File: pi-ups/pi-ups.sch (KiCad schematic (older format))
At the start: 31 parts, among them J1 , Q1 IRLML2244, Q2 IRLML2244, Q3 IRLML2244, Q4 IRLML2244, U1 BMS_1S, U2 DC-DC, U3 BMS_1S, U4 FTDI232, U5 Arduino_Pro_Mini

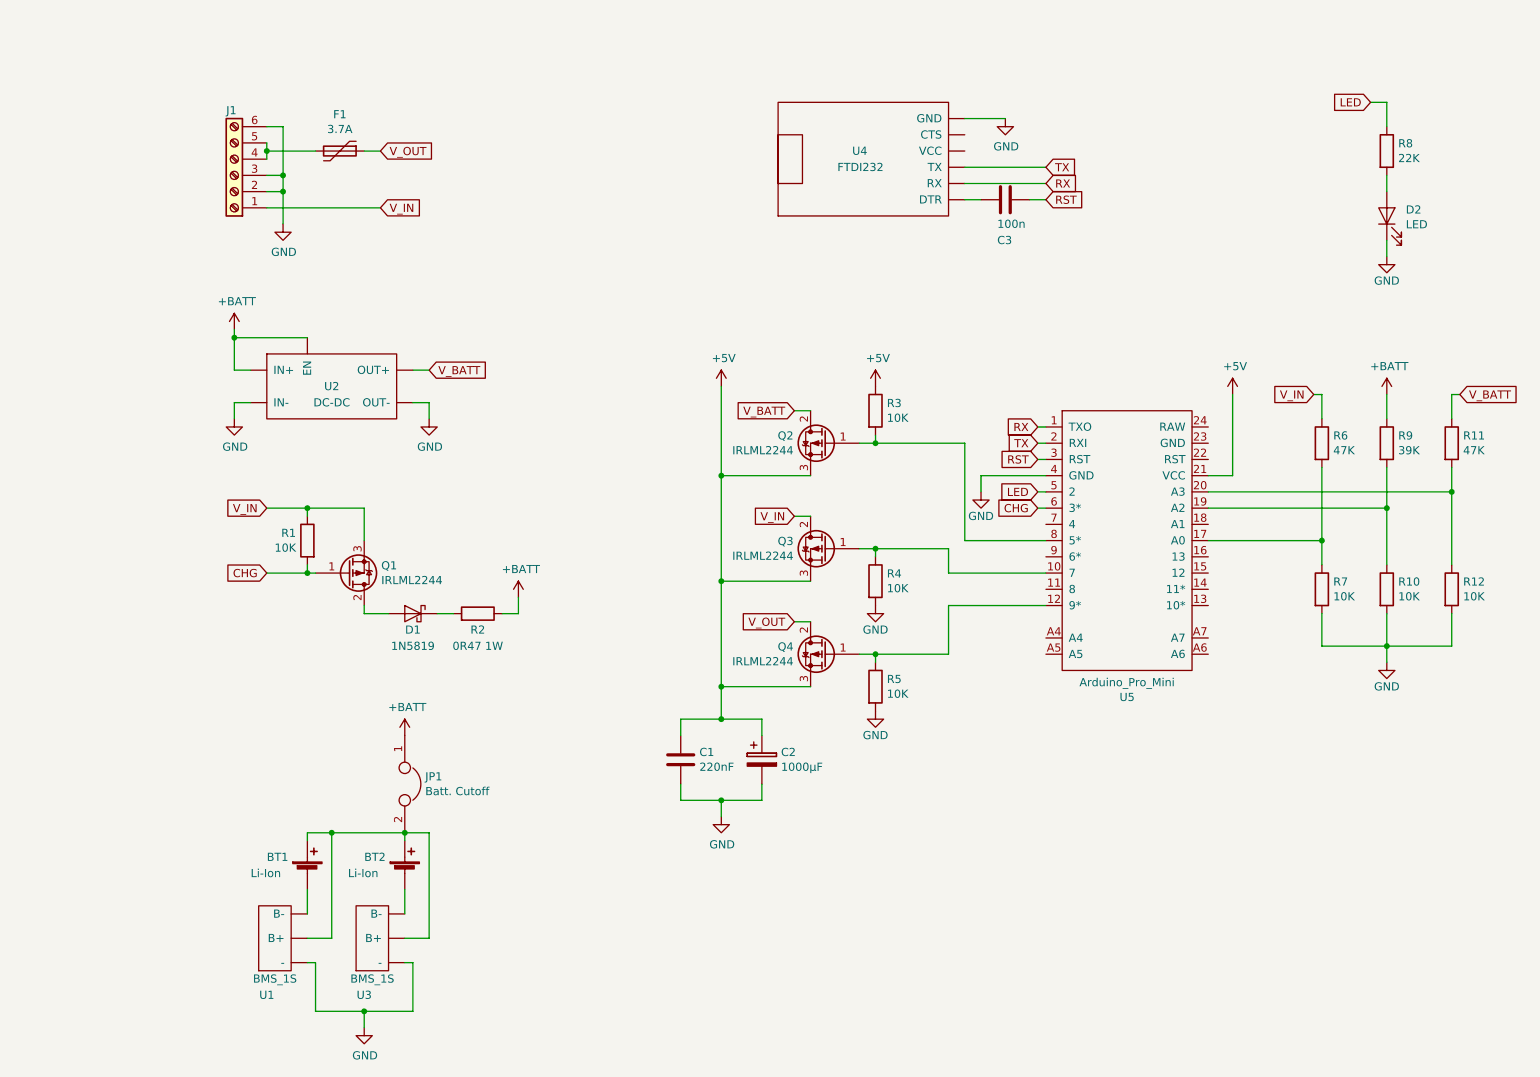
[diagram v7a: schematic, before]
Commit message: pi-ups: rotate Arduino
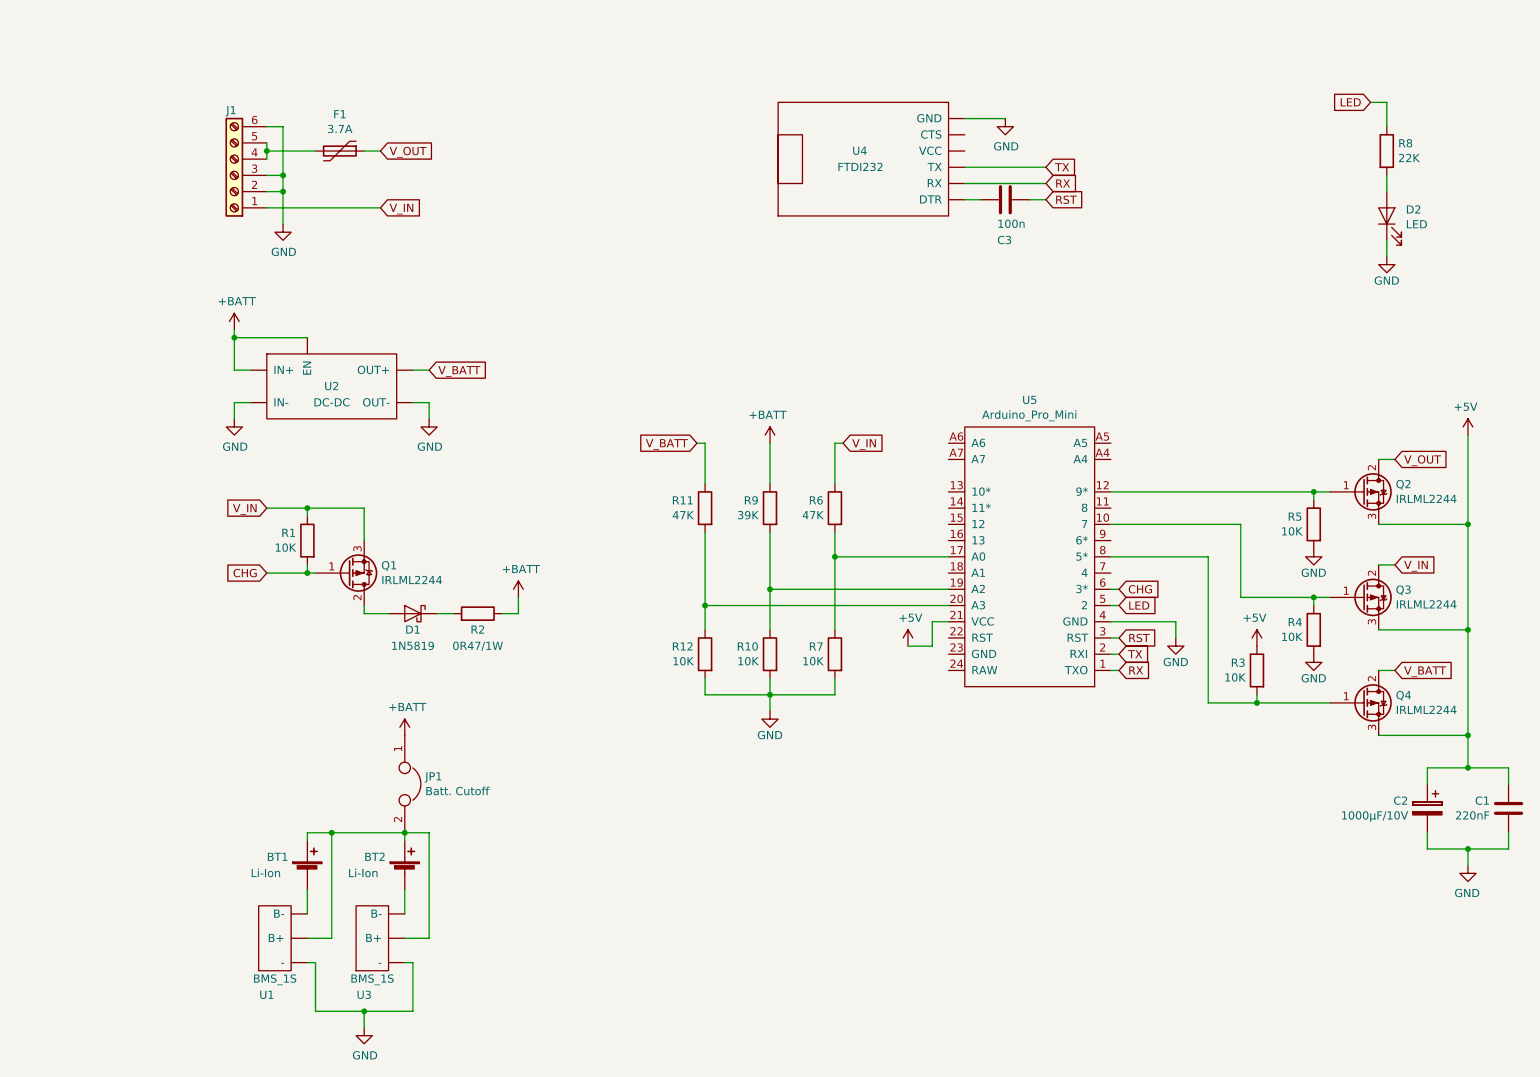
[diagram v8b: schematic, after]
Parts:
- C2: value 1000µF -> 1000µF/10V
- R2: value 0R47 1W -> 0R47/1W
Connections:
- net V_BATT: now also Q4.2 (D); no longer Q2.2 (D)
- net V_OUT: now also Q2.2 (D); no longer Q4.2 (D)
- net at R5.1, U5.12 (9*): now also Q2.1 (G); no longer Q4.1 (G)
- net at R3.2, U5.8 (5*): now also Q4.1 (G); no longer Q2.1 (G)
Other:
- moved on the sheet: C1, C2, Q2, Q3, Q4, R10, R11, R12, R3, R4, R5, R6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
